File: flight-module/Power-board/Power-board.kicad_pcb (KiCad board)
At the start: 4 copper layers, 141.7 x 134.1 mm, 30 parts, among them J1 POWER, J10 PCIE, J2 PCIE, J3 XT60-M, J4 PCIE, J5 PCIE, J6 ESP32-DEVKITC-32D, J7 Conn_01x19_Male, J8 PCIE, J9 Conn_01x19_Male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

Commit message: Merged power board
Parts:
- removed D1: D_Small, Diode_SMD:D_0603_1608Metric
- removed F4: 6A Fuse, Fuse:Fuse_2920_7451Metric
- removed G***: LOGO, star:star_8x7
- removed J10, J2, J4: PCIE, 10018784-10210TLF:AMPHENOL_10018784-10210TLF
- removed J3: XT60-M, XT60-M:AMASS_XT60-M
- removed J6: ESP32-DEVKITC-32D, Ellie_Project_Footprints:MODULE_ESP32-DEVKITC-32D
- removed J7, J9: Conn_01x19_Male, Connector_PinHeader_2.54mm:PinHeader_1x19_P2.54mm_Vertical
- removed R2: 1k, Resistor_SMD:R_0603_1608Metric
- removed REF**: DSUB-15_Female_Horizontal_P2.77x2.84mm_EdgePinOffset14.56mm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, Connector_Dsub:DSUB-15_Female_Horizontal_P2.77x2.84mm_EdgePinOffset14.56mm_Housed_MountingHolesOffset15.98mm
- removed REF**: Stack_Shape, Stack_Shape:Stack_Shape
- removed SW1: SW_SPST, Button_Switch_THT:SW_PUSH_6mm
- removed U2: 74HC4050D, 74HC4050D:SO16
- added C10: 22nF, Capacitor_SMD:C_0603_1608Metric, F.Cu at (131.7, 89.4)
- added C11: 0.1µF, Capacitor_SMD:C_0603_1608Metric, F.Cu at (138.4, 92.0)
- added C12: 10uF, Capacitor_SMD:C_0603_1608Metric, F.Cu at (152.4, 92.7)
- added C6: 22uF, Capacitor_SMD:C_0603_1608Metric, F.Cu at (148.7, 82.7)
- added C8: 22nF, Capacitor_SMD:C_0603_1608Metric, F.Cu at (131.7, 82.5)
- added C9: 22nF, Capacitor_SMD:C_0603_1608Metric, F.Cu at (131.7, 86.8)
- added D15: D_Schottky, D_Schottky:SMADO-214AC_LEAD-FRAME_MCC, F.Cu at (157.2, 95.7)
- added D16: D_Schottky, D_Schottky:SMADO-214AC_LEAD-FRAME_MCC, F.Cu at (80.0, 100.8)
- added D2: D_Small, Diode_SMD:D_0603_1608Metric, F.Cu at (143.5, 85.2)
- added R3: 10k, Resistor_SMD:R_0603_1608Metric, F.Cu at (147.7, 86.0)
- C4: value 22uF -> 22nF
- J1: value POWER -> Stack_Shape; footprint Connector:Banana_Jack_2Pin -> Stack_Shape:Stack_Shape
- J5: value PCIE -> POWER; footprint 10018784-10210TLF:AMPHENOL_10018784-10210TLF -> Connector:Banana_Jack_2Pin; moved to F.Cu
- J8: value PCIE -> XT60-M; footprint 10018784-10210TLF:AMPHENOL_10018784-10210TLF -> Connector_AMASS:AMASS_XT60PW-F_1x02_P7.20mm_Horizontal; moved to F.Cu
- R1: value 10k -> 1k
- U1, U4: footprint AZ1117IH-3:SOT230P700X185-4N -> AZ1117IH-3:SOT223_AZ1117I_6P5X3P5_DIO
- U3: value XTSD04GLGEAG -> TPS4H160BQPWPRQ1; footprint XTSD04GLGEAG:SON127P600X800X95-8N -> TPS4:PWP0028C_N
- moved C1 233.0 mm to (77.6, 70.4), turned to 90 degrees
- moved C3 232.4 mm to (78.0, 81.0), turned to 90 degrees
- moved F2 232.2 mm to (82.2, 69.6)
- moved F3 232.1 mm to (82.1, 80.3)
- moved U1 231.2 mm to (89.2, 71.1), turned to -90 degrees
- moved U4 231.1 mm to (89.2, 81.8), turned to -90 degrees
- moved C2 225.3 mm to (89.1, 76.2), turned to 180 degrees
- moved C5 224.8 mm to (89.2, 87.8), turned to 180 degrees
- moved J1 217.9 mm to (123.2, 86.1), turned to 0 degrees
- moved C4 184.2 mm to (131.7, 79.6), turned to 0 degrees
- moved U3 172.2 mm to (121.9, 84.8)
- moved F1 165.7 mm to (156.6, 83.8), turned to 0 degrees
- moved R1 165.4 mm to (152.4, 97.3)
- moved J5 158.0 mm to (139.3, 37.8), turned to 180 degrees
- moved J8 95.8 mm to (153.2, 52.1)
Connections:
- C1 pad 2: 3.3V -> +3.3V
- C2 pad 2: 12V -> V_ALL+
- C3 pad 2: 5V -> +5V
- C4 pad 1: GND -> LOX_VENT+
- C4 pad 2: Net-(C4-Pad2) -> GND
- C5 pad 2: 12V -> V_ALL+
- F1 pad 1: +12V -> /BAT1_+_pre
- F1 pad 2: Net-(C4-Pad2) -> /BAT1_+
- F2 pad 2: 3.3V -> +3.3V
- F3 pad 2: 5V -> +5V
- R1 pad 1: Net-(C4-Pad2) -> Net-(C12-Pad1)
- R1 pad 2: Net-(D1-Pad1) -> GND
- U1 pad 3: 12V -> V_ALL+
- U3 pad 1: unconnected-(U3-Pad1) -> GND
- U3 pad 2: SD CS_3.3 -> unconnected-(U3-NC-Pad2)
- U3 pad 3: SD CLK_3.3 -> PYRO1EN
- U3 pad 4: GND -> PYRO2EN
- U3 pad 5: SD MOSI_3.3 -> PYRO3EN
- U3 pad 6: SD, TC MISO -> PYRO4EN
- U3 pad 8: 3.3V -> unconnected-(U3-ST2_SEL_N-Pad8)
- U4 pad 3: 12V -> V_ALL+
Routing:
- net 12V: track 363.1 -> 0.00 mm, vias 3 -> 0
- net 3.3V: track 293.4 -> 0.00 mm, vias 5 -> 0
- net GND: track 350.6 -> 61.7 mm, vias 24 -> 20
- net HX CLK: track 262.4 -> 0.00 mm, vias 10 -> 0
- net HX3: track 262.4 -> 0.00 mm, vias 10 -> 0
- net SD, TC MISO: track 262.3 -> 0.00 mm, vias 9 -> 0
- net HX5: track 256.1 -> 0.00 mm, vias 7 -> 0
- net SD, TC CLK: track 241.9 -> 0.00 mm, vias 15 -> 0
- net HX7: track 241.6 -> 0.00 mm, vias 11 -> 0
- net TC2: track 240.4 -> 0.00 mm, vias 7 -> 0
- net HX1: track 237.9 -> 0.00 mm, vias 8 -> 0
- net HX6: track 236.2 -> 0.00 mm, vias 10 -> 0
- net HX8: track 233.8 -> 0.00 mm, vias 10 -> 0
- net TC CLK: track 223.3 -> 0.00 mm, vias 11 -> 0
- net TC MISO: track 215.4 -> 0.00 mm, vias 10 -> 0
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- added copper zone on In1.Cu, net GND
- added copper zone on F.Cu, net V_ALL+
- added copper zone on In2.Cu, net V_ALL+
- removed copper zone on B.Cu, net GND
- removed copper zone on F.Cu, net GND
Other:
- board text removed: "+"
- board text removed: "-"
- board text removed: "3V3"
- board text removed: "A1"
- board text removed: "B1"
- board text removed: "Banana plug"
- board text removed: "Designed by: Khai Sam"
- board text removed: "EN"
- board text removed: "ESP32-DEVKITC-V4"
- board text removed: "GND"
- board text removed: "Ground DAQ 2 LE2 Hotfire 2023"
- board text removed: "HX CLK"
- board text removed: "HX1 DT"
- board text removed: "HX2 DT"
- board text removed: "HX3 DT"
- board text removed: "HX4 DT"
- board text removed: "HX5 DT"
- board text removed: "HX6 DT"
- board text removed: "HX7 DT"
- board text removed: "HX8 DT"
- board text removed: "I2C SCL"
- board text removed: "I2C SDA"
- board text removed: "PERIPHERAL 1"
- board text removed: "PERIPHERAL 2"
- board text removed: "PERIPHERAL 3"
- board text removed: "PERIPHERAL 4"
- board text removed: "PERIPHERAL 5"
- board text removed: "SD CLK"
- board text removed: "SD CS"
- board text removed: "SD MISO"
- board text removed: "SD MOSI"
- board text removed: "TC CLK"
- board text removed: "TC MISO"
- board text removed: "TC1 CS"
- board text removed: "TC2 CS"
- board text removed: "TC3 CS"
- board text removed: "TC4 CS"
- board text removed: "This side up"
- board text removed: "Wrong side"
- board text removed: "XT-60"

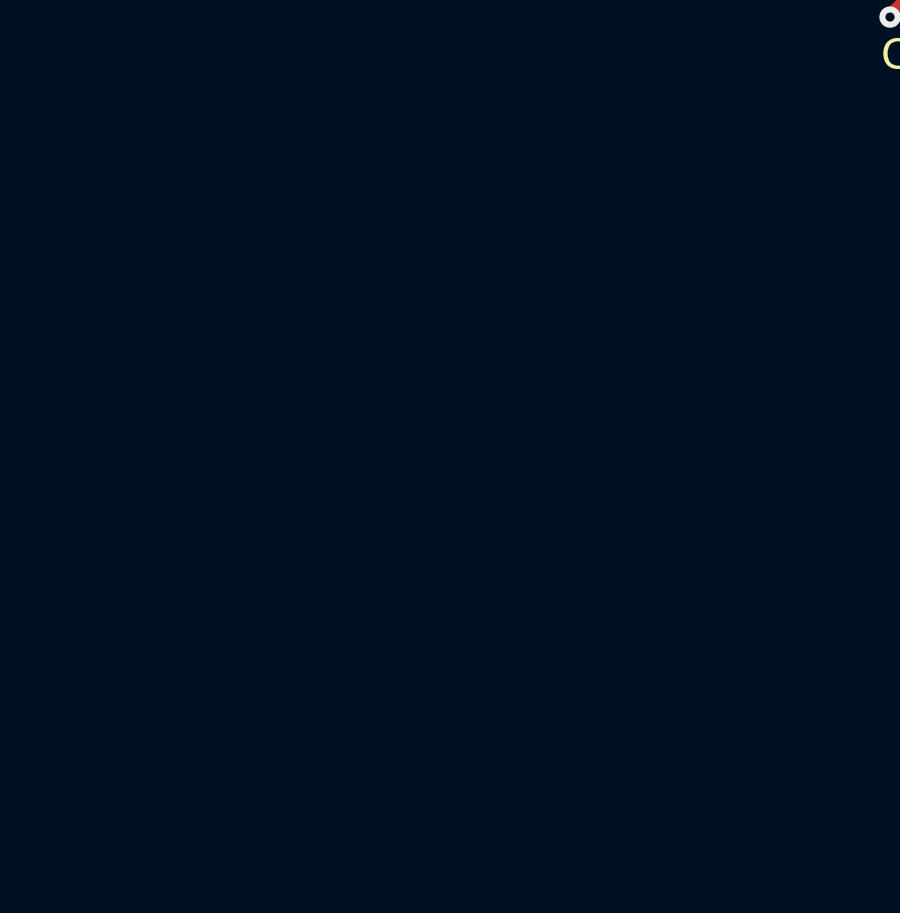
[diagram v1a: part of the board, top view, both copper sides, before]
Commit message: added star logo onto power board
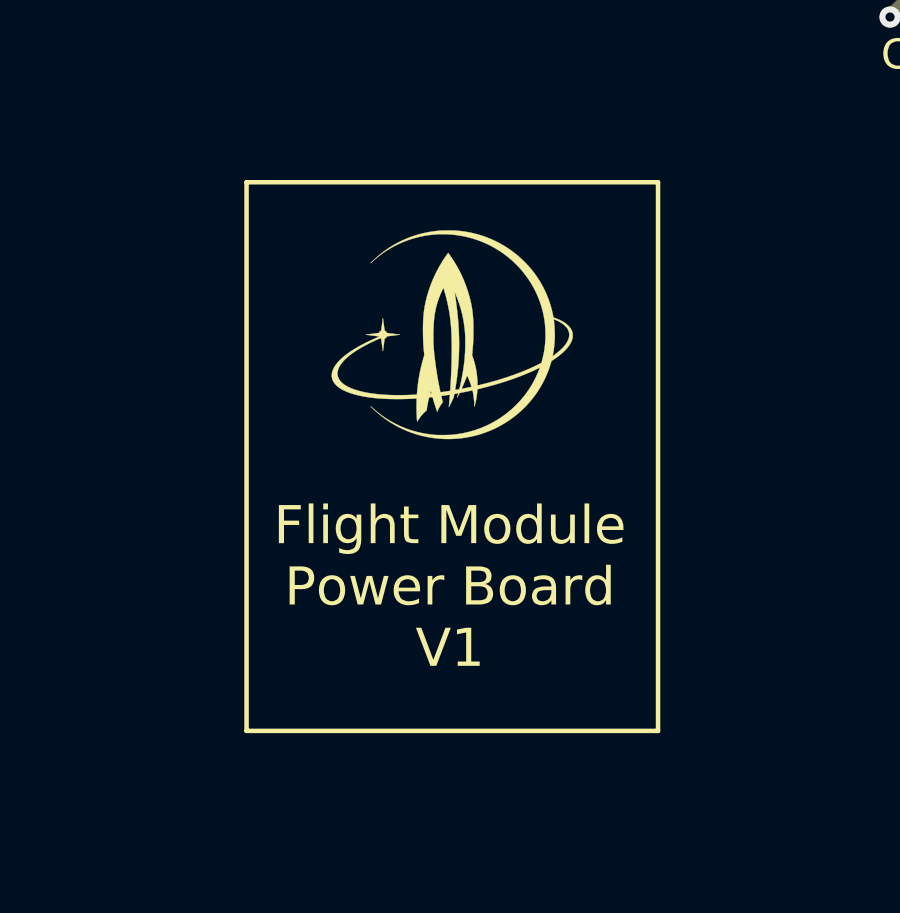
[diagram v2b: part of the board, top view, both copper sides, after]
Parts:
- added G***: LOGO, star:star_8x7, F.Cu at (121.5, 103.3)
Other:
- board text added: "Flight Module Power Board V1"

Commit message: fixed some power board issues
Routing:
- net ETH_VENT+: track 73.3 -> 72.7 mm
- net ETH_MAIIN+: track 6.81 -> 6.21 mm
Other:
- board text added: "+"
- board text added: "-"
